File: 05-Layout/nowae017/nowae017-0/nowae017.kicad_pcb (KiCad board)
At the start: 2 copper layers, 52.1 x 27.2 mm, 34 parts, among them P1 CONN_9X1, P2 CONN_9X1, P3 NANOSIM, P4 ESIM, P5 U.FL, Q1 PTDC114EU, Q2 PTDC114EU, U3 PCA9306DC, U4 SARA-U201

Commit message: WiP placement (nowae017-0)
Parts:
- added DL3: RED, LEDs:LED-0603, F.Cu at (178.9, 90.6)
- added G***: LOGO, LOGO:LOGO_NOWAE_10MM_FSILK, F.Cu at (124.1, 98.1)
- added R12: 2k2, RESISTOR:RESISTOR-0402, F.Cu at (178.9, 91.8)
- added U1: TPS73501DRV, SON:WSON6_2.0x2.0_0.65_6+1, F.Cu at (156.7, 102.6)
- added U2: TXB0108DQSR, SON:USON20_4.0x2.0_0.4_20, F.Cu at (157.0, 96.8)
- P1: moved to B.Cu
- R5: footprint RESISTOR:RESISTOR-1210 -> RESISTOR:RESISTOR-1206
- moved C10 97.6 mm to (124.6, 80.5), turned to 180 degrees
- moved C11 93.9 mm to (124.6, 82.4), turned to 180 degrees
- moved F1 84.8 mm to (151.2, 103.8)
- moved R8 74.0 mm to (151.6, 82.0), turned to 180 degrees
- moved C2 73.2 mm to (160.5, 103.6), turned to 90 degrees
- moved R4 72.2 mm to (159.9, 101.8)
- moved R5 71.7 mm to (165.6, 103.5)
- moved R3 71.5 mm to (159.3, 103.6), turned to 90 degrees
- moved C7 70.9 mm to (151.6, 80.9), turned to 180 degrees
- moved DL1 70.2 mm to (171.4, 100.3)
- moved C3 67.0 mm to (162.2, 103.1), turned to 90 degrees
- moved R7 66.6 mm to (151.6, 83.1), turned to 180 degrees
- moved C1 66.2 mm to (153.8, 103.1), turned to 270 degrees
- moved C4 66.0 mm to (158.4, 82.0), turned to 180 degrees
- moved Q2 65.5 mm to (175.9, 101.6)
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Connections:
- C3 pad 1: +3.8V -> Net-(C2-Pad1)
- U4 pad 33: Net-(U4-Pad33) -> GND
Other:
- board size 52.1 x 27.2 mm -> 52.1 x 25.4 mm
- copper layers 2 -> 4
- net class Default: trace_width 0.25 -> 0.2; via_dia 0.8 -> 0.6; via_drill 0.4 -> 0.3

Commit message: Placement complete (nowae017-0)
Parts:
- moved R9 38.1 mm to (156.5, 100.3)
- moved R1 25.8 mm to (158.3, 83.1)
- moved C5 22.6 mm to (159.6, 87.3), turned to 270 degrees
- moved Q2 19.7 mm to (156.6, 97.7)
- moved Q1 19.5 mm to (156.6, 93.0)
- moved C6 18.5 mm to (155.1, 87.4), turned to 90 degrees
- moved R10 16.9 mm to (156.5, 90.8), turned to 180 degrees
- moved DL3 16.1 mm to (169.1, 103.4), turned to 90 degrees
- moved R11 15.8 mm to (156.5, 95.5), turned to 180 degrees
- moved DL1 14.8 mm to (158.7, 92.7), turned to 90 degrees
- moved DL2 13.8 mm to (158.7, 97.4), turned to 90 degrees
- moved R12 13.0 mm to (169.1, 100.4), turned to 90 degrees
- moved R2 11.5 mm to (158.3, 84.3)
- moved U2 9.65 mm to (157.3, 87.2), turned to 180 degrees
- moved P3 0.87 mm to (165.6, 87.3)
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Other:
- board size 52.1 x 25.4 mm -> 49.5 x 25.4 mm

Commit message: WiP: routing (nowae017-0)
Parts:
- moved C6 0.66 mm to (154.4, 87.3)
- moved R2 0.53 mm to (158.8, 84.0)
- moved R1 0.51 mm to (158.8, 82.9)
- moved C4 0.45 mm to (158.8, 81.8)
- moved R6 0.45 mm to (158.8, 80.7)
- moved C5 0.35 mm to (159.9, 87.3)
- moved C7 0.20 mm to (151.6, 80.7)
- moved R8 0.20 mm to (151.6, 81.8)
- moved R7 0.20 mm to (151.6, 82.9)
- moved U3 0.10 mm to (155.2, 81.6)
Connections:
- U2 pad 2: /UART_RXD_EXT -> /UART_TXD_EXT
- U2 pad 3: /UART_RXD_EXT -> /UART_CTS_EXT
- U2 pad 4: /UART_RXD_EXT -> /UART_RTS_EXT
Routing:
- net /UART_RI_EXT: track 0.00 -> 41.0 mm, vias 0 -> 1
- net /UART_RTS_EXT: track 0.00 -> 37.1 mm, vias 0 -> 1
- net /UART_CTS_EXT: track 0.00 -> 35.5 mm, vias 0 -> 1
- net /UART_TXD_EXT: track 0.00 -> 31.0 mm, vias 0 -> 1
- net /UART_RI: track 0.00 -> 30.4 mm, vias 0 -> 2
- net /UART_RXD_EXT: track 0.00 -> 28.3 mm, vias 0 -> 1
- net /UART_RTS: track 0.00 -> 26.7 mm, vias 0 -> 2
- net /UART_CTS: track 0.00 -> 25.2 mm, vias 0 -> 2
- net /UART_TXD: track 0.00 -> 24.3 mm, vias 0 -> 2
- net /SARA_GPIO4_EXT: track 0.00 -> 23.7 mm, vias 0 -> 1
- net /SARA_GPIO3_EXT: track 0.00 -> 23.4 mm, vias 0 -> 1
- net /UART_RXD: track 0.00 -> 22.7 mm, vias 0 -> 2
- net GND: track 0.00 -> 17.4 mm
- net +1.8V: track 0.07 -> 7.65 mm
- net Net-(C4-Pad2): track 0.00 -> 4.35 mm
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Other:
- net class Default: clearance 0.2 -> 0.1
- rule trace_clearance: 0.2 -> 0.1

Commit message: WiP routing (nowae017-0)
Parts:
- added R13: 0, RESISTOR:RESISTOR-0402, F.Cu at (155.3, 83.2)
- added R14: 0, RESISTOR:RESISTOR-0402, F.Cu at (155.3, 84.3)
- moved R1 0.30 mm to (158.8, 82.6)
- moved R7 0.30 mm to (151.6, 82.6)
- moved C4 0.30 mm to (158.8, 81.5)
- moved C7 0.30 mm to (151.6, 80.4)
- moved R6 0.30 mm to (158.8, 80.4)
- moved R8 0.30 mm to (151.6, 81.5)
- moved U3 0.30 mm to (155.2, 81.3)
- moved R2 0.25 mm to (158.8, 83.8)
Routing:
- net /UART_RI_EXT: track 41.0 -> 0.00 mm, vias 1 -> 0
- net /SARA_GPIO4_EXT: track 23.7 -> 0.00 mm, vias 1 -> 0
- net /SARA_GPIO3_EXT: track 23.4 -> 0.00 mm, vias 1 -> 0
- net /PCM_DIN: track 0.00 -> 18.1 mm
- net /I2C_SCL: track 1.95 -> 19.1 mm, vias 0 -> 2
- net /PCM_CLK: track 0.00 -> 16.9 mm
- net /I2C_SDA: track 2.56 -> 19.4 mm, vias 0 -> 2
- net /PCM_DOUT: track 0.00 -> 15.5 mm
- net /SARA_TX_LED: track 0.00 -> 14.2 mm, vias 0 -> 2
- net /PCM_SYNC: track 0.00 -> 14.1 mm
- net /SARA_PWRON: track 0.00 -> 13.7 mm, vias 0 -> 2
- net /SARA_GPIO3: track 0.00 -> 13.6 mm, vias 0 -> 2
- net /SARA_GPIO4: track 1.90 -> 14.2 mm, vias 1 -> 2
- net /SARA_STS_LED: track 0.00 -> 4.00 mm
- net /UART_RXD: track 22.7 -> 26.0 mm
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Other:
- net class Default: clearance 0.1 -> 0.15; trace_width 0.2 -> 0.15
- rule pad_to_mask_clearance: 0.2 -> 0
- rule trace_clearance: 0.1 -> 0.15
- rule trace_min: 0.2 -> 0.15
- rule via_min_size: 0.4 -> 0.6

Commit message: WiP routing (nowae017-0)
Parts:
- moved F1 0.52 mm to (151.3, 104.3)
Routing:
- added copper zone on F.Cu, net +VIN
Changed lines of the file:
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@@
     (user_trace_width 1)
     (trace_clearance 0.15)
-    (zone_clearance 0.508)
+    (zone_clearance 0.2)
     (zone_45_only no)
     (trace_min 0.15)
@@
   )
   (module RESISTOR:RESISTOR-0603 (layer F.Cu)
-    (at 151.2 103.8)
+    (at 151.35 104.3)
     (descr "SMD 0603")
     (tags "0603 SM0603")
@@
   (segment (start 143.49 99.16) (end 145.3 97.35) (width 0.15) (layer In1.Cu) (net 61))
   (segment (start 158.154 85.354) (end 158.529587 85.354) (width 0.2) (layer F.Cu) (net 65))
+  (zone (net 12) (net_name +VIN) (layer F.Cu) (hatch edge 0.508)
+    (connect_pads yes (clearance 0.2))
+    (min_thickness 0.2)
+    (fill yes (arc_segments 16) (thermal_gap 0.1) (thermal_bridge_width 0.1))
+    (polygon
+      (pts
+        (xy 147.75 100.85) (xy 151 100.85) (xy 151 105.1) (xy 147.65 105.15) (xy 147.65 100.85)
+      )
+    )
+  )
 )

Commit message: WiP: routing (nowae017-0)
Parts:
- moved C8 8.34 mm to (160.5, 97.6), turned to 90 degrees
- moved R12 3.33 mm to (169.6, 103.7), turned to 180 degrees
- moved DL3 1.14 mm to (169.6, 102.4), turned to 0 degrees
- moved P4 0.21 mm to (163.9, 97.8), turned to 90 degrees
- moved C1 0.15 mm to (153.8, 103.2)
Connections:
- R1 pad 2: +3.3V -> +VDIO
- R2 pad 2: +3.3V -> +VDIO
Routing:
- net /I2C_SCL_EXT: track 4.17 -> 47.4 mm, vias 0 -> 1
- net /I2C_SDA_EXT: track 4.77 -> 46.3 mm, vias 0 -> 1
- net /UART_RI_EXT: track 0.00 -> 41.4 mm, vias 0 -> 1
- net /SIM_VCC: track 3.54 -> 43.9 mm, vias 0 -> 2
- net +1.8V: track 7.65 -> 47.2 mm, vias 0 -> 2
- net /SIM_IO: track 0.00 -> 38.1 mm, vias 0 -> 2
- net +VDIO: track 2.26 -> 38.4 mm, vias 0 -> 1
- net /SIM_RST: track 0.00 -> 32.9 mm, vias 0 -> 3
- net /SIM_CLK: track 0.00 -> 28.2 mm, vias 0 -> 2
- net /SARA_GPIO4_EXT: track 0.00 -> 22.1 mm, vias 0 -> 1
- net /SARA_GPIO3_EXT: track 0.00 -> 20.9 mm, vias 0 -> 1
- net GND: track 17.4 -> 11.8 mm
- net Net-(C2-Pad2): track 0.00 -> 4.19 mm
- net /CODEC_CLK: track 0.00 -> 2.97 mm
- net /I2C_SCL: track 19.1 -> 17.7 mm
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- added copper zone on F.Cu, net Net-(C1-Pad1)
- added copper zone on F.Cu, net Net-(C2-Pad1)

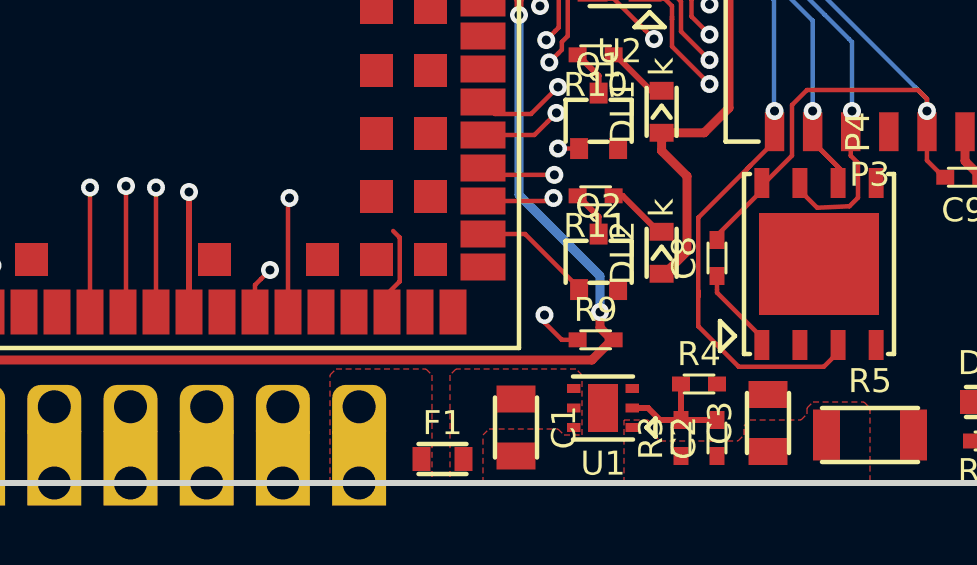
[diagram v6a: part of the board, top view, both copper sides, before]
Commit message: WiP routing of supply zone (nowae017-0)
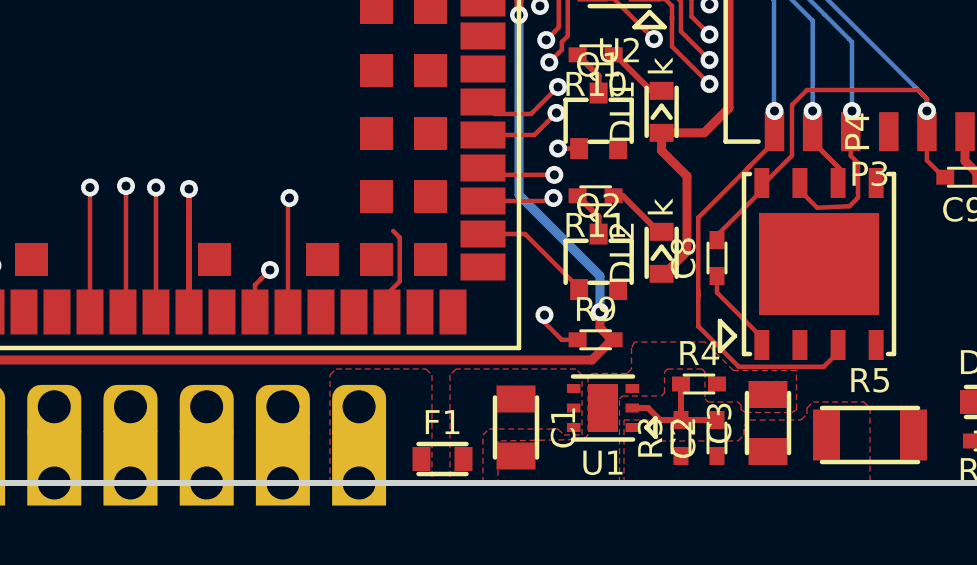
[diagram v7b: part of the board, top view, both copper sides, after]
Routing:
- net /UART_RXD: track 26.0 -> 24.3 mm
- added copper zone on F.Cu, net GND
